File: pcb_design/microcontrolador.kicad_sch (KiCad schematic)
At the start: 28 parts, among them J1 DB128L-5.08-2P-BK-S, U1 ESP32-S3-WROOM-1(N16R8), U2 TYPE-C 16PLT-H10.0

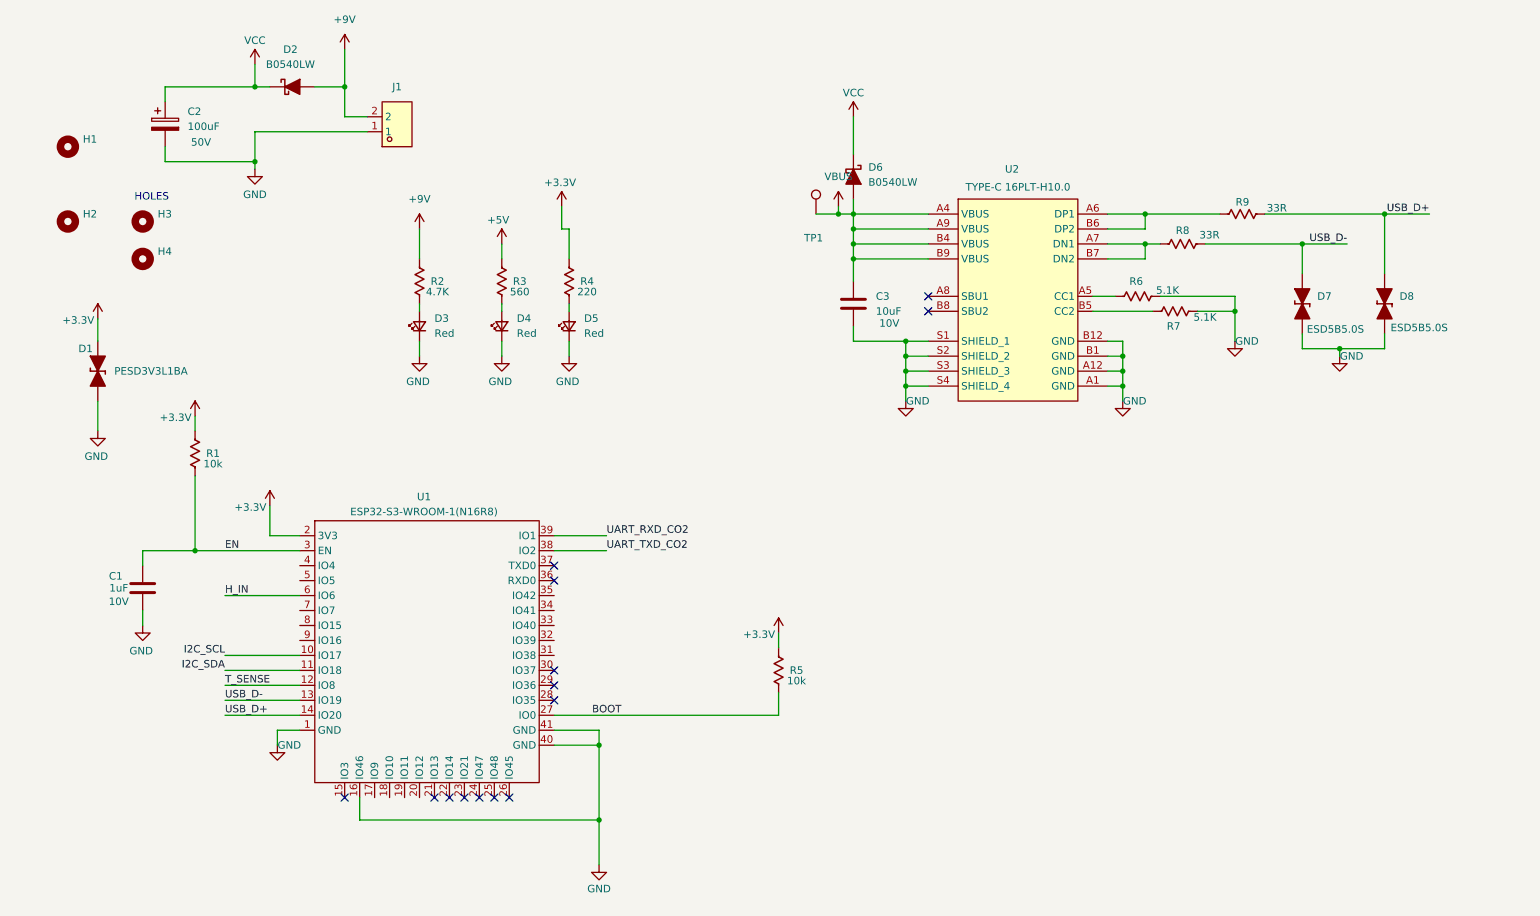
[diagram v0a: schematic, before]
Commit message: cambio de regulador de alto iq por reguladores de bajo iq separados uno para sensores y otro para micro y comunicacion usando el lt8610, apagado de alimentacion de sensores atravez de mosfet canal p
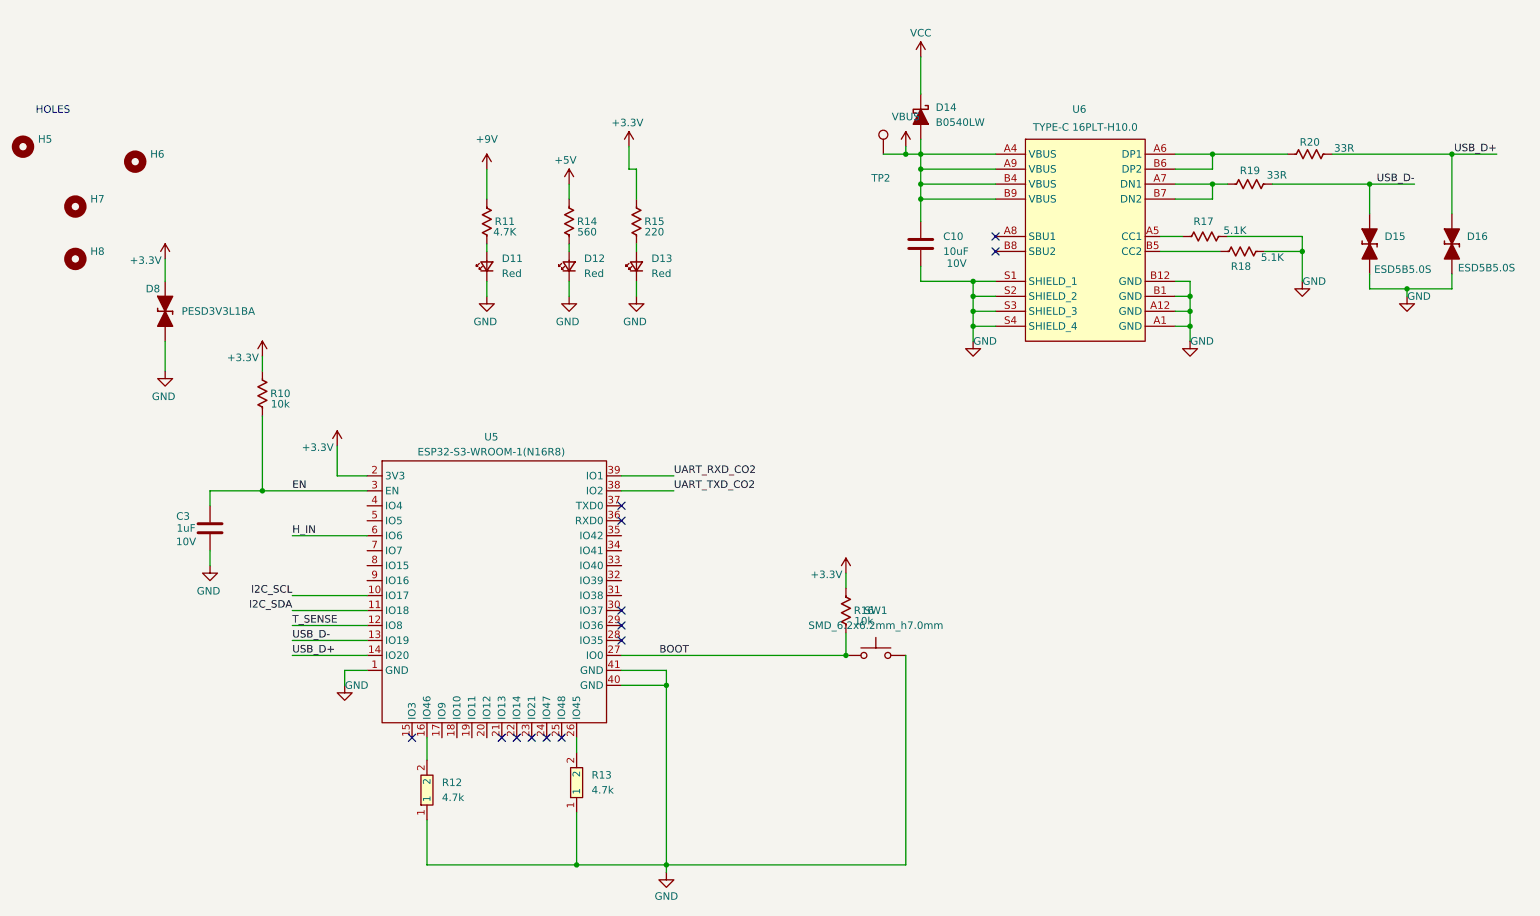
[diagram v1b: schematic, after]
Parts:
- removed C1: 1uF, Capacitor_SMD_AKL:C_0603_1608Metric, symbol PCM_Capacitor_US_AKL:C_0603
- removed C2: 100uF, Capacitor_SMD_AKL:CP_Elec_6.3x7.7, symbol Capacitor_AKL:CP_SMD_D6.3mm_H7.7mm
- removed C3: 10uF, PCM_Capacitor_SMD_AKL:C_0805_2012Metric, symbol PCM_Capacitor_AKL:C_0805
- removed D1: PESD3V3L1BA, Diode_SMD_AKL:D_SOD-323_TVS, symbol PCM_Diode_TVS_AKL:PESD3V3L1BA
- removed D2: B0540LW, Diode_SMD_AKL:D_SOD-123, symbol PCM_Diode_Schottky_AKL:B0540LW
- removed D3, D4, D5: Red, SparkFun-LED:LED_0603_1608Metric_Red, symbol SparkFun-LED:LED_Red_0603
- removed D6: B0540LW, PCM_Diode_SMD_AKL:D_SOD-123, symbol PCM_Diode_Schottky_AKL:B0540LW
- removed D7, D8: ESD5B5.0S, PCM_Diode_SMD_AKL:D_SOD-523, symbol PCM_Diode_TVS_AKL:ESD5B5.0S
- removed H1, H2, H3, H4: MountingHole, MountingHole:MountingHole_2.2mm_M2, symbol Mechanical:MountingHole
- removed J1: DB128L-5.08-2P-BK-S, EasyEDA:CONN-TH_2P-P5.08_DB128L-5.08-2P-BK-S, symbol EasyEDA:DB128L-5.08-2P-BK-S
- removed R1: 10k, Resistor_SMD_AKL:R_0603_1608Metric, symbol PCM_Resistor_US_AKL:R_0603
- removed R2: 4.7K, Resistor_SMD_AKL:R_0603_1608Metric, symbol PCM_Resistor_US_AKL:R_0603
- removed R3: 560, Resistor_SMD_AKL:R_0603_1608Metric, symbol PCM_Resistor_US_AKL:R_0603
- removed R4: 220, Resistor_SMD_AKL:R_0603_1608Metric, symbol PCM_Resistor_US_AKL:R_0603
- removed R5: 10k, PCM_Resistor_SMD_AKL:R_0603_1608Metric, symbol PCM_Resistor_US_AKL:R_0603
- removed R6, R7: 5.1K, PCM_Resistor_SMD_AKL:R_0603_1608Metric, symbol PCM_Resistor_US_AKL:R_0603
- removed R8, R9: 33R, PCM_Resistor_SMD_AKL:R_0603_1608Metric, symbol PCM_Resistor_US_AKL:R_0603
- removed TP1: TestPoint_Hole1, 4ms_TestPoint:TestPoint_WireHole, symbol MG_ELECTROMECANICAL:TestPoint_Hole1
- removed U1: ESP32-S3-WROOM-1(N16R8), EasyEDA:WIRELM-SMD_ESP32-S3-WROOM-1, symbol EasyEDA:ESP32-S3-WROOM-1(N16R8)
- removed U2: TYPE-C 16PLT-H10.0, EasyEDA:TYPE-C-SMD_USB4120-03-C, symbol EasyEDA:TYPE-C16PLT-H10.0
- added C10: 10uF, PCM_Capacitor_SMD_AKL:C_0805_2012Metric, symbol PCM_Capacitor_AKL:C_0805
- added C3: 1uF, Capacitor_SMD_AKL:C_0603_1608Metric, symbol PCM_Capacitor_US_AKL:C_0603
- added D11, D12, D13: Red, SparkFun-LED:LED_0603_1608Metric_Red, symbol SparkFun-LED:LED_Red_0603
- added D14: B0540LW, PCM_Diode_SMD_AKL:D_SOD-123, symbol PCM_Diode_Schottky_AKL:B0540LW
- added D15, D16: ESD5B5.0S, PCM_Diode_SMD_AKL:D_SOD-523, symbol PCM_Diode_TVS_AKL:ESD5B5.0S
- added D8: PESD3V3L1BA, Diode_SMD_AKL:D_SOD-323_TVS, symbol PCM_Diode_TVS_AKL:PESD3V3L1BA
- added H5, H6, H7, H8: MountingHole, MountingHole:MountingHole_2.2mm_M2, symbol Mechanical:MountingHole
- added R10: 10k, Resistor_SMD_AKL:R_0603_1608Metric, symbol PCM_Resistor_US_AKL:R_0603
- added R11: 4.7K, Resistor_SMD_AKL:R_0603_1608Metric, symbol PCM_Resistor_US_AKL:R_0603
- added R12, R13: 4.7k, EasyEDA:R0603, symbol EasyEDA:RC0603FR-074K7L
- added R14: 560, Resistor_SMD_AKL:R_0603_1608Metric, symbol PCM_Resistor_US_AKL:R_0603
- added R15: 220, Resistor_SMD_AKL:R_0603_1608Metric, symbol PCM_Resistor_US_AKL:R_0603
- added R16: 10k, PCM_Resistor_SMD_AKL:R_0603_1608Metric, symbol PCM_Resistor_US_AKL:R_0603
- added R17, R18: 5.1K, PCM_Resistor_SMD_AKL:R_0603_1608Metric, symbol PCM_Resistor_US_AKL:R_0603
- added R19, R20: 33R, PCM_Resistor_SMD_AKL:R_0603_1608Metric, symbol PCM_Resistor_US_AKL:R_0603
- added SW1: SMD_6.2x6.2mm_h7.0mm, PCM_SparkFun-Switch:Push_SMD_6.2x6.2mm, symbol PCM_SparkFun-Switch:SPST_Push_SMD_6.2x6.2mm_h7.0mm
- added TP2: TestPoint_Hole1, 4ms_TestPoint:TestPoint_WireHole, symbol MG_ELECTROMECANICAL:TestPoint_Hole1
- added U5: ESP32-S3-WROOM-1(N16R8), EasyEDA:WIRELM-SMD_ESP32-S3-WROOM-1, symbol EasyEDA:ESP32-S3-WROOM-1(N16R8)
- added U6: TYPE-C 16PLT-H10.0, EasyEDA:TYPE-C-SMD_USB4120-03-C, symbol EasyEDA:TYPE-C16PLT-H10.0
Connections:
- net +3.3V: now also D8.2 (A), R10.1, R15.1, R16.1, U5.2 (3V3)
- net +5V: now also R14.1
- net +9V: now also R11.1
- net BOOT: now also R16.2, SW1.1, U5.27 (IO0)
- net EN: now also C3.2, R10.2, U5.3 (EN)
- net GND: now also C10.2, C3.1, D11.1 (K), D12.1 (K), D13.1 (K), D15.1 (K), D16.1 (K), D8.1 (K), R12.1, R13.1, R17.2, R18.2, SW1.2, U5.1 (GND), U5.40 (GND), U5.41 (GND), U6.A1 (GND), U6.A12 (GND), U6.B1 (GND), U6.B12 (GND), U6.S1 (SHIELD_1), U6.S2 (SHIELD_2), U6.S3 (SHIELD_3), U6.S4 (SHIELD_4)
- net H_IN: now also U5.6 (IO6)
- net I2C_SCL: now also U5.10 (IO17)
- net I2C_SDA: now also U5.11 (IO18)
- net T_SENSE: now also U5.12 (IO8)
- net UART_RXD_CO2: now also U5.39 (IO1)
- net UART_TXD_CO2: now also U5.38 (IO2)
- net USB_D+: now also D16.2 (A), R20.2, U5.14 (IO20)
- net USB_D-: now also D15.2 (A), R19.2, U5.13 (IO19)
- net VBUS: now also C10.1, D14.2 (A), TP2.1, U6.A4 (VBUS), U6.A9 (VBUS), U6.B4 (VBUS), U6.B9 (VBUS)
- net VCC: now also D14.1 (K)
- new net: R19.1, U6.A7 (DN1), U6.B7 (DN2)
- new net: D11.2 (A), R11.2
- new net: R20.1, U6.A6 (DP1), U6.B6 (DP2)
- new net: D13.2 (A), R15.2
- new net: R13.2, U5.26 (IO45)
- new net: R12.2, U5.16 (IO46)
- new net: R17.1, U6.A5 (CC1)
- new net: R18.1, U6.B5 (CC2)
- new net: D12.2 (A), R14.2
- no-connect marks 14 -> 13
